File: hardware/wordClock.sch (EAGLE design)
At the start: 38 parts, among them J1 SPI_PRG, Q1 MOSFET-PCHANNELSMD, Q2 MOSFET-PCHANNELSMD, Q3 MOSFET-PCHANNELSMD, Q4 MOSFET-PCHANNELSMD, Q5 MOSFET-PCHANNELSMD, Q6 MOSFET-PCHANNELSMD, Q7 MOSFET-PCHANNELSMD, Q8 MOSFET-PCHANNELSMD, SW1 HR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

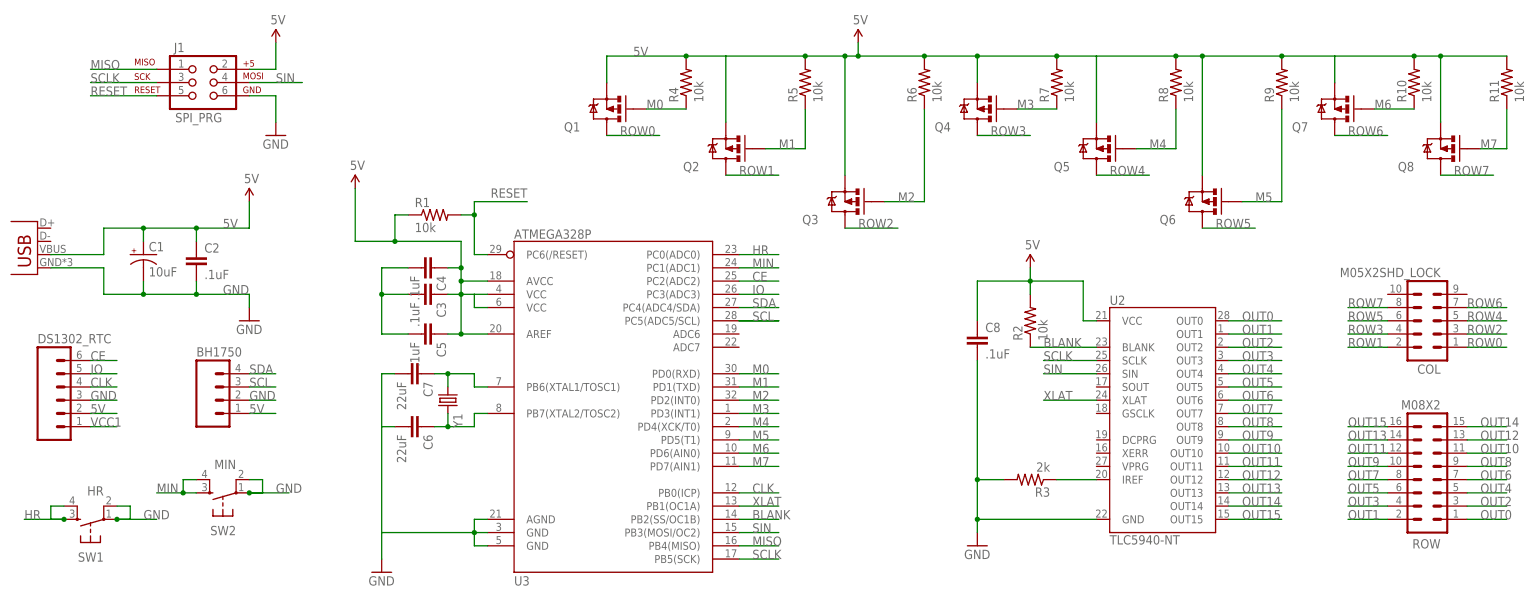
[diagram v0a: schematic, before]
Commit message: Fixed floating nets
There was a floating net around the crystal, SCL was named SLI on a pin,
and various ERC errors fixed.
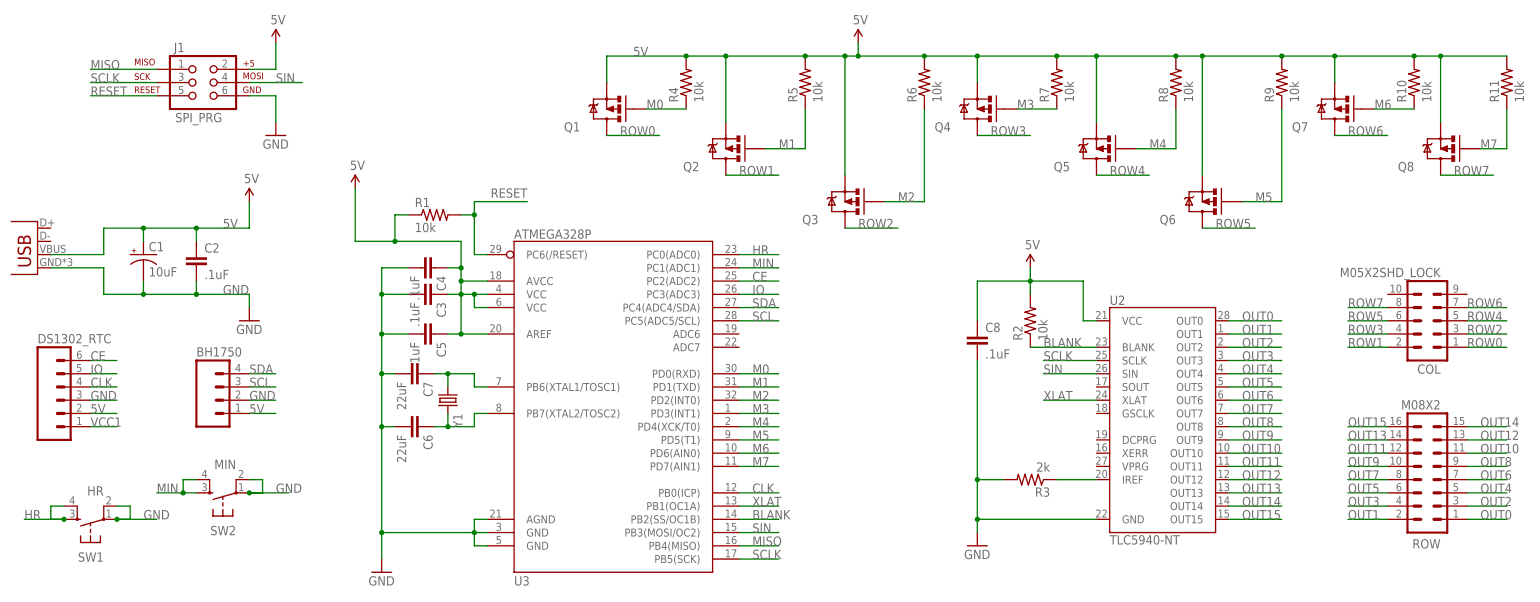
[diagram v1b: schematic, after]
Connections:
- removed net N$5: C3.2, C4.2, C5.2
- net GND: now also C3.2, C4.2, C5.2
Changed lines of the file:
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@@
 <pinref part="GND1" gate="1" pin="GND"/>
 <wire x1="63.5" y1="15.24" x2="63.5" y2="10.16" width="0.1524" layer="91"/>
+<pinref part="C4" gate="G$1" pin="2"/>
+<wire x1="68.58" y1="66.04" x2="63.5" y2="66.04" width="0.1524" layer="91"/>
+<pinref part="C3" gate="G$1" pin="2"/>
+<wire x1="68.58" y1="60.96" x2="63.5" y2="60.96" width="0.1524" layer="91"/>
+<wire x1="63.5" y1="60.96" x2="63.5" y2="66.04" width="0.1524" layer="91"/>
+<junction x="63.5" y="60.96"/>
+<pinref part="C5" gate="G$1" pin="2"/>
+<wire x1="68.58" y1="53.34" x2="63.5" y2="53.34" width="0.1524" layer="91"/>
+<wire x1="63.5" y1="53.34" x2="63.5" y2="60.96" width="0.1524" layer="91"/>
+<wire x1="63.5" y1="53.34" x2="63.5" y2="45.72" width="0.1524" layer="91"/>
+<junction x="63.5" y="45.72"/>
+<junction x="63.5" y="15.24"/>
+<junction x="63.5" y="35.56"/>
+<junction x="63.5" y="53.34"/>
 </segment>
 </net>
@@
 <wire x1="38.1" y1="43.18" x2="43.18" y2="43.18" width="0.1524" layer="91"/>
 <label x="38.1" y="43.18" size="1.778" layer="95"/>
-</segment>
-<segment>
-<pinref part="U3" gate="G$1" pin="PC5(ADC5/SCL)"/>
-<wire x1="132.08" y1="55.88" x2="139.7" y2="55.88" width="0.1524" layer="91"/>
 </segment>
 <segment>
@@
 <junction x="78.74" y="60.96"/>
 <junction x="78.74" y="63.5"/>
+<junction x="81.28" y="60.96"/>
 </segment>
 <segment>
@@
 <junction x="154.94" y="106.68"/>
 <label x="111.76" y="106.68" size="1.778" layer="95"/>
+<junction x="200.66" y="106.68"/>
+<junction x="246.38" y="106.68"/>
+<junction x="129.54" y="106.68"/>
 </segment>
 <segment>
@@
 </segment>
 </net>
-<net name="N$5" class="0">
-<segment>
-<pinref part="C4" gate="G$1" pin="2"/>
-<wire x1="68.58" y1="66.04" x2="63.5" y2="66.04" width="0.1524" layer="91"/>
-<pinref part="C3" gate="G$1" pin="2"/>
-<wire x1="68.58" y1="60.96" x2="63.5" y2="60.96" width="0.1524" layer="91"/>
-<wire x1="63.5" y1="60.96" x2="63.5" y2="66.04" width="0.1524" layer="91"/>
-<junction x="63.5" y="60.96"/>
-<pinref part="C5" gate="G$1" pin="2"/>
-<wire x1="68.58" y1="53.34" x2="63.5" y2="53.34" width="0.1524" layer="91"/>
-<wire x1="63.5" y1="53.34" x2="63.5" y2="60.96" width="0.1524" layer="91"/>
-</segment>
-</net>
